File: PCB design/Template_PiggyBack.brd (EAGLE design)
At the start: 63.5 x 88.6 mm, 46 parts, among them CN1 USB power supply, IC1 MCP6002, IC3 MCP6002, IC4 REG1117

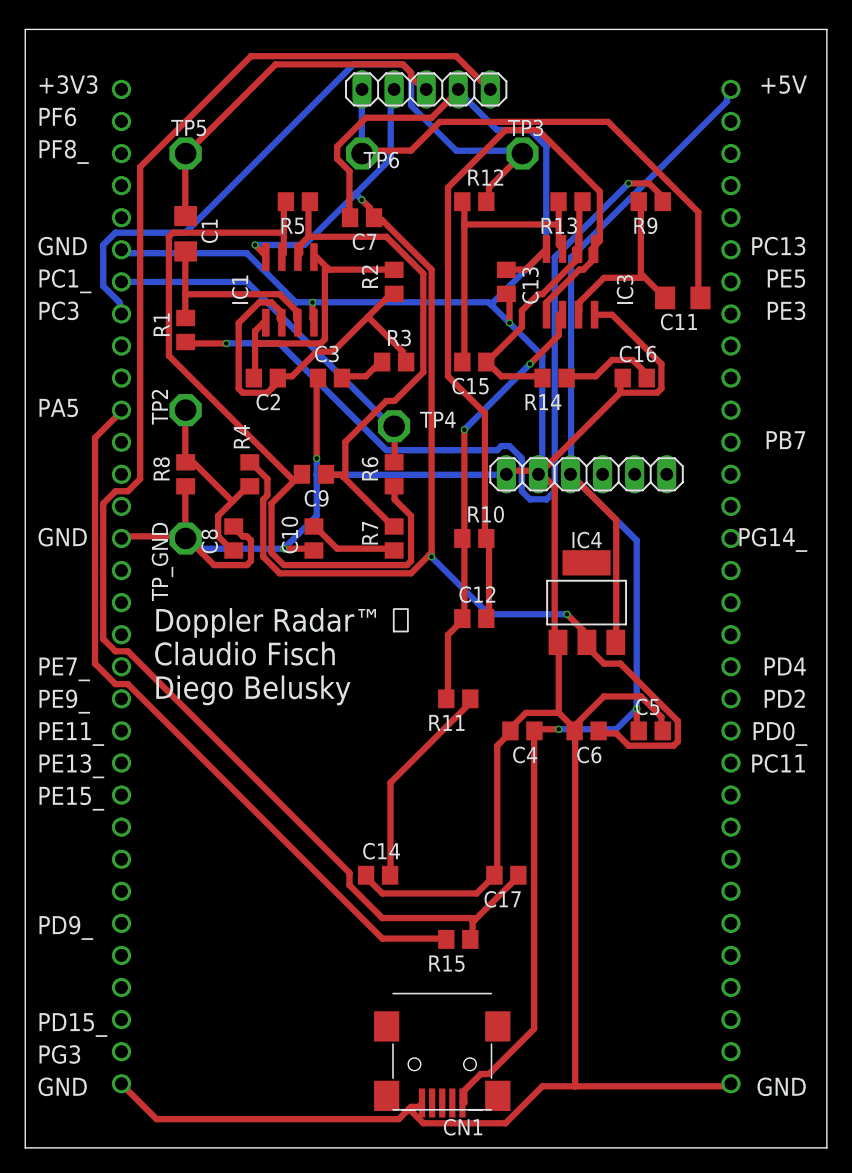
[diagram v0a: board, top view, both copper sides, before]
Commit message: GND plate added
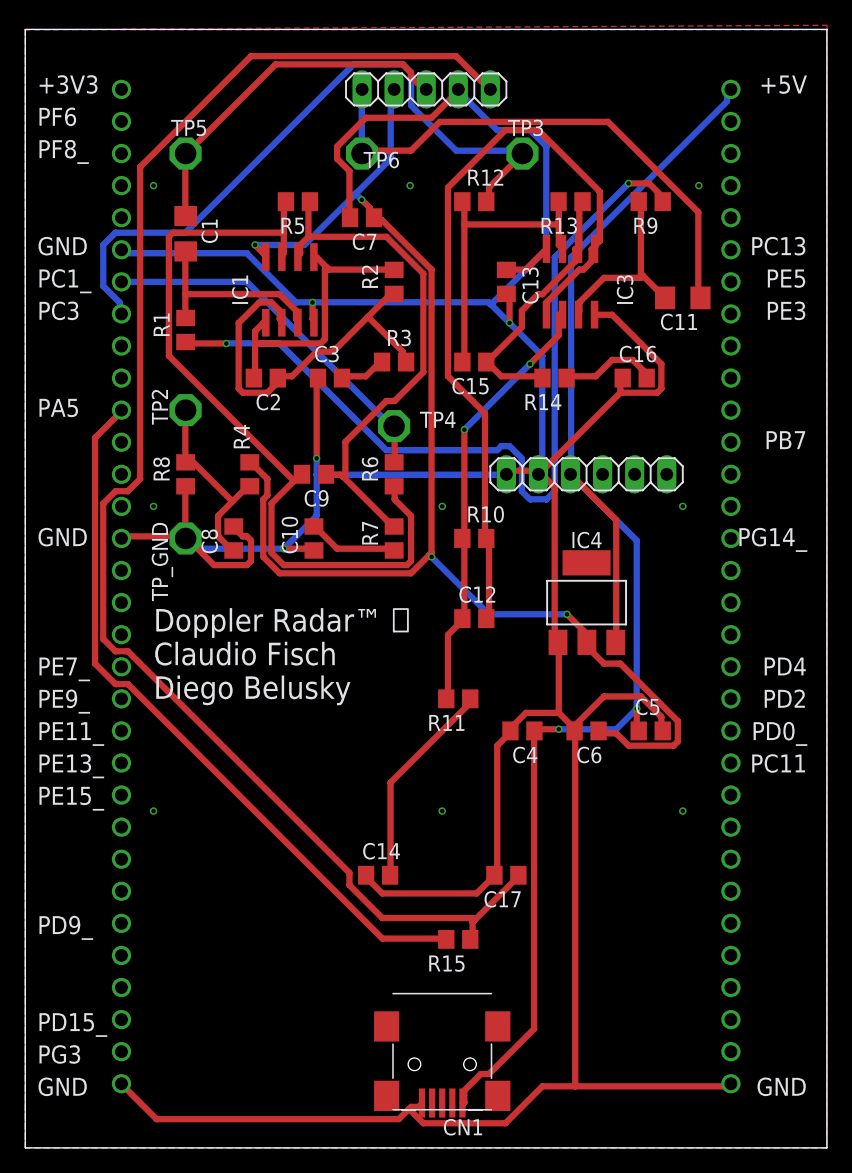
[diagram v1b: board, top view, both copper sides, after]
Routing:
- net GND: vias 4 -> 13
- added copper zone on layer 1, net GND
- added copper zone on layer 16, net GND
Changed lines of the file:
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@@
 <via x="38.35" y="65.325" extent="1-16" drill="0.35"/>
 <via x="22.75" y="66.95" extent="1-16" drill="0.35"/>
+<polygon width="0.1524" layer="16" isolate="0.016">
+<vertex x="63.5" y="0"/>
+<vertex x="63.5" y="88.55"/>
+<vertex x="0" y="88.55"/>
+<vertex x="0" y="0"/>
+</polygon>
+<polygon width="0.1524" layer="1" isolate="0.016">
+<vertex x="0" y="88.55"/>
+<vertex x="63.5" y="88.9"/>
+<vertex x="63.5" y="0"/>
+<vertex x="0" y="0"/>
+</polygon>
+<via x="10.16" y="76.2" extent="1-16" drill="0.35"/>
+<via x="30.48" y="76.2" extent="1-16" drill="0.35"/>
+<via x="53.34" y="76.2" extent="1-16" drill="0.35"/>
+<via x="10.16" y="50.8" extent="1-16" drill="0.35"/>
+<via x="33.02" y="50.8" extent="1-16" drill="0.35"/>
+<via x="52.07" y="50.8" extent="1-16" drill="0.35"/>
+<via x="10.16" y="26.67" extent="1-16" drill="0.35"/>
+<via x="33.02" y="26.67" extent="1-16" drill="0.35"/>
+<via x="52.07" y="26.67" extent="1-16" drill="0.35"/>
 </signal>
 <signal name="PF6">

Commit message: errors fixed
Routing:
- net GND: track 316.7 -> 0.00 mm, vias 13 -> 0
- net VCO: track 117.5 -> 74.7 mm, vias 0 -> 1
- net N$7: track 62.5 -> 34.1 mm, vias 0 -> 2
- net +3V3: track 109.2 -> 91.1 mm, vias 4 -> 2
- net N$9: track 34.6 -> 50.4 mm, vias 2 -> 0
- net N$8: track 41.2 -> 52.5 mm
- net +5V: track 114.2 -> 103.1 mm, vias 2 -> 0
- net N$12: track 63.4 -> 52.9 mm
- net N$2: track 31.2 -> 21.6 mm
- net V_GND: track 67.0 -> 59.9 mm, vias 2 -> 0
- net PC1_: track 29.2 -> 34.0 mm
- net PC3: track 54.7 -> 50.6 mm
- net IF_Q: track 42.5 -> 38.6 mm
- net PA5: track 57.8 -> 55.1 mm
- net N$11: track 15.4 -> 16.8 mm, vias 0 -> 2
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
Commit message: layout done
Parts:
- added C18: 100n, rcl:C0805
- moved C14 40.5 mm to (49.5, 55.9)
- moved R15 31.4 mm to (17.8, 43.2)
- moved R11 30.7 mm to (49.5, 62.2)
- moved C12 22.2 mm to (44.5, 62.2), turned to 180 degrees
- moved C17 22.2 mm to (33.0, 43.2)
- moved R14 21.9 mm to (45.7, 82.5)
- moved C16 21.7 mm to (50.8, 82.5)
- moved C15 20.9 mm to (40.6, 82.5)
- moved R10 14.5 mm to (39.4, 62.2), turned to 180 degrees
- moved C7 8.98 mm to (17.8, 74.9), turned to 90 degrees
- moved TP3 4.02 mm to (35.6, 80.0)
- moved JP8 3.81 mm to (44.5, 49.5)
- moved C11 3.59 mm to (49.5, 69.8), turned to 90 degrees
- moved C13 2.54 mm to (35.6, 68.6)
- moved IC3 2.54 mm to (40.6, 68.6)
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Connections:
- removed net N$6: C8.1, R4.1, R8.2, TP2.TP
- net +3V3: now also C18.1
- net GND: now also C18.2
- net V_GND: now also C8.1, R4.1, R8.2, TP2.TP
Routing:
- net N$9: track 50.4 -> 15.5 mm
- net PA5: track 55.1 -> 20.5 mm
- net N$12: track 52.9 -> 21.5 mm
- net N$6: track 17.1 -> 0.00 mm
- net N$7: track 34.1 -> 48.3 mm, vias 2 -> 0
- net N$15: track 16.7 -> 6.35 mm
- net N$14: track 21.3 -> 14.7 mm
- net VCO: track 74.7 -> 69.8 mm
- net N$13: track 24.3 -> 19.4 mm
- net IF_Q: track 38.6 -> 34.3 mm, vias 0 -> 1
- net V_GND: track 59.9 -> 62.4 mm, vias 0 -> 1
- net PC1_: track 34.0 -> 36.4 mm
- net PC3: track 50.6 -> 48.4 mm, vias 0 -> 1
- net +3V3: track 91.1 -> 89.1 mm, vias 2 -> 0
- net N$10: track 8.64 -> 6.92 mm
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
